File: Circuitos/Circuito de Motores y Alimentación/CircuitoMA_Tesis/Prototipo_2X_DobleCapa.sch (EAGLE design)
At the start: 28 parts, among them Q1 IRLZ44Z, Q2 IRLZ44Z, Q3 IRLZ44Z, Q4 IRLZ44Z, X1 22-23-2021

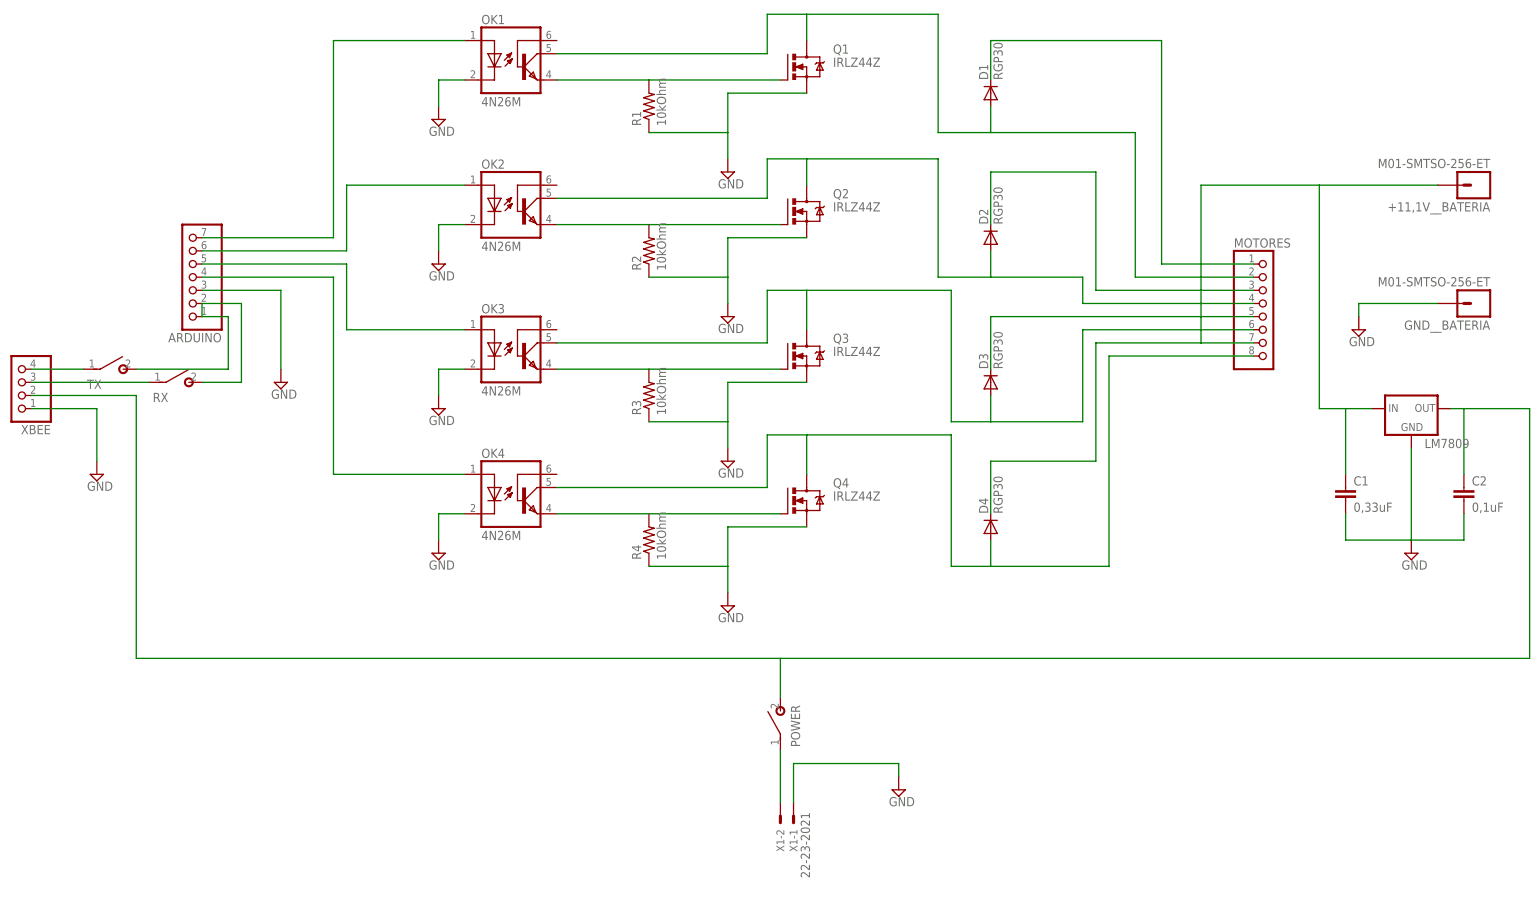
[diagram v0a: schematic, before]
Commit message: Circuito
Circuito de motores y alimentación doble capa
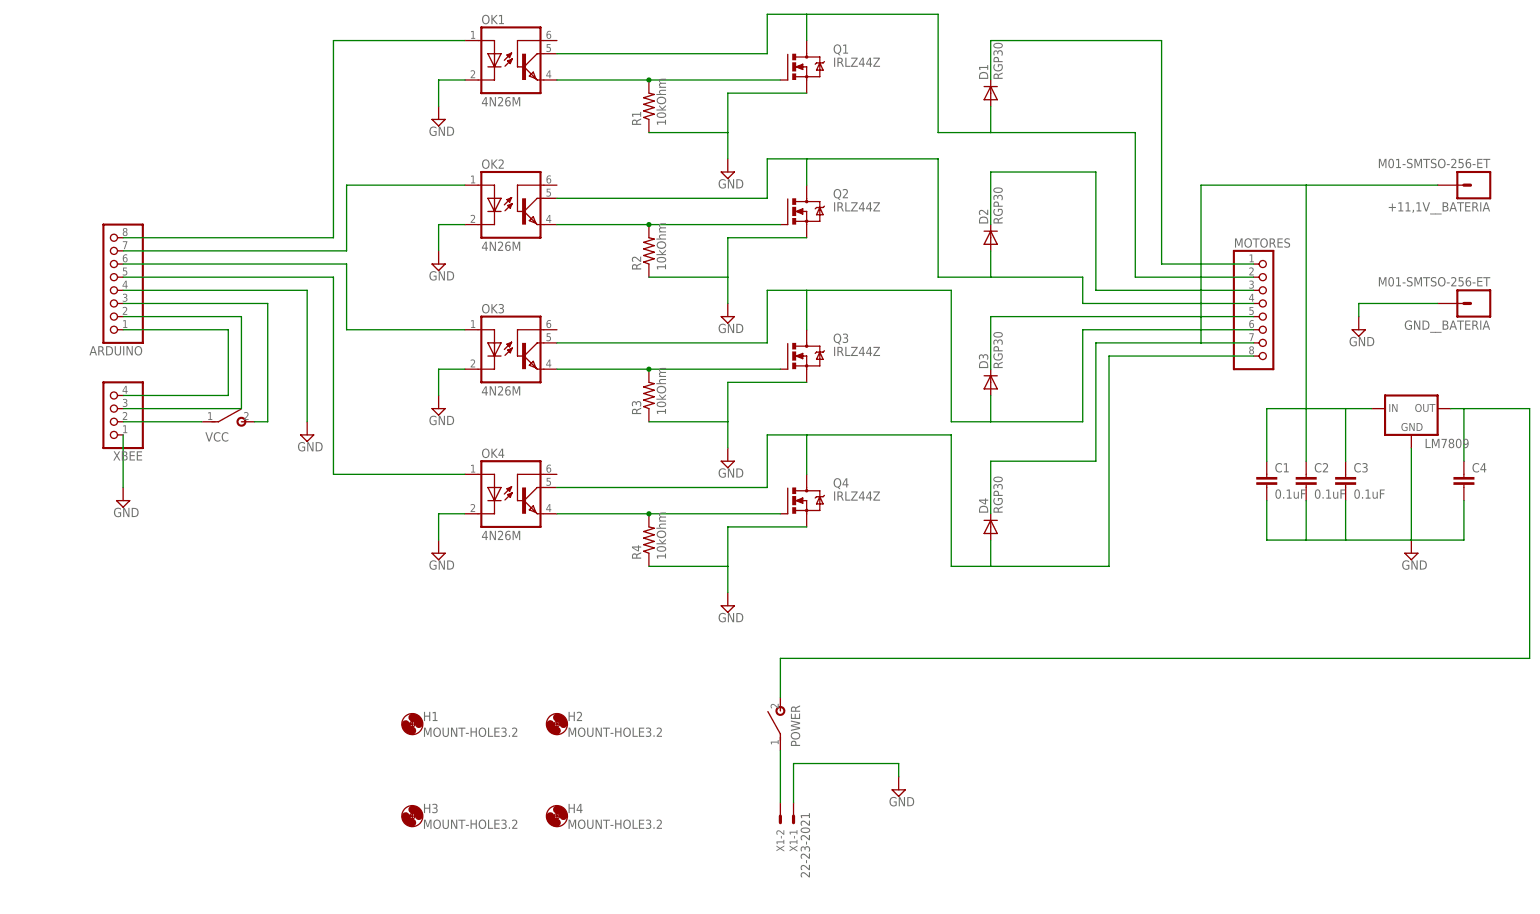
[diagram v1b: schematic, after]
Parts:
- removed RX, TX: SPST, gm-switches:SPST
- added C3: 0.1uF, SparkFun-Capacitors:0.1UF-50V-20%(PTH)KIT-EZ
- added C4: (no value), SparkFun-Capacitors:0.1UF-50V-20%(PTH)KIT-EZ
- added H1, H2, H3, H4: MOUNT-HOLE3.2, holes:MOUNT-HOLE3.2
- added VCC: SPST, gm-switches:SPST
- ARDUINO: device pinhead:PINHD-1X7/90 -> pinhead:PINHD-1X8/90
- C1: value 0,33uF -> 0.1uF; device rcl:C-EU050-030X075 -> SparkFun-Capacitors:0.1UF-50V-20%(PTH)KIT-EZ; PROD_ID (none) -> CAP-08370
- C2: value 0,1uF -> 0.1uF; device rcl:C-EU050-030X075 -> SparkFun-Capacitors:0.1UF-50V-20%(PTH)KIT-EZ; PROD_ID (none) -> CAP-08370
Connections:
- new net N$20: ARDUINO.3, VCC.S
- net GND: now also ARDUINO.4, C3.2, C4.2; no longer ARDUINO.3
- net N$1: now also ARDUINO.8; no longer ARDUINO.7
- net N$11: now also R4.2
- net N$12: now also C2.1, C3.1
- net N$13: now also ARDUINO.2; no longer RX.P
- net N$2: now also ARDUINO.7; no longer ARDUINO.6
- net N$3: now also ARDUINO.6; no longer ARDUINO.5
- net N$4: now also ARDUINO.5; no longer ARDUINO.4
- net N$5: now also ARDUINO.1; no longer TX.P
- net N$6: now also C4.1; no longer C2.1, XBEE.2
- net N$7: now also VCC.P, XBEE.2; no longer ARDUINO.1, ARDUINO.2, RX.S, TX.S
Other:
- moved on the sheet: C1, C2, XBEE

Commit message: Circuito
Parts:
- removed POWER, VCC: SPST, gm-switches:SPST
- removed X1: 22-23-2021, con-molex:22-23-2021
- added JP1: (no value), pinhead:PINHD-1X2
- added JP2: (no value), pinhead:PINHD-1X2/90
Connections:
- removed net N$6: C4.1, LM7809.OUT, POWER.S
- net GND: now also JP2.1; no longer X1-1.S
- net N$18: now also C4.1, JP2.2, LM7809.OUT; no longer POWER.P, X1-2.S
- net N$20: now also JP1.1; no longer VCC.S
- net N$7: now also JP1.2; no longer VCC.P
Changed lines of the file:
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@@
 <part name="GND__BATERIA" library="SparkFun-Connectors" deviceset="M01" device="-SMTSO-256-ET"/>
 <part name="SUPPLY12" library="supply2" deviceset="GND" device=""/>
-<part name="POWER" library="gm-switches" deviceset="SPST" device=""/>
-<part name="X1" library="con-molex" deviceset="22-23-2021" device=""/>
 <part name="SUPPLY13" library="supply2" deviceset="GND" device=""/>
 <part name="R4" library="rcl" deviceset="R-US_" device="0207/7" value="10kOhm"/>
 <part name="ARDUINO" library="pinhead" deviceset="PINHD-1X8" device="/90"/>
 <part name="R1" library="rcl" deviceset="R-US_" device="0207/7" value="10kOhm"/>
-<part name="VCC" library="gm-switches" deviceset="SPST" device=""/>
 <part name="C3" library="SparkFun-Capacitors" deviceset="0.1UF-50V-20%(PTH)" device="KIT-EZ" value="0.1uF"/>
 <part name="C1" library="SparkFun-Capacitors" deviceset="0.1UF-50V-20%(PTH)" device="KIT-EZ" value="0.1uF">
@@
 <part name="H3" library="holes" deviceset="MOUNT-HOLE" device="3.2"/>
 <part name="H4" library="holes" deviceset="MOUNT-HOLE" device="3.2"/>
+<part name="JP2" library="pinhead" deviceset="PINHD-1X2" device="/90"/>
+<part name="JP1" library="pinhead" deviceset="PINHD-1X2" device=""/>
 </parts>
 <sheets>
@@
 <instance part="GND__BATERIA" gate="G$1" x="208.28" y="35.56" rot="R180"/>
 <instance part="SUPPLY12" gate="GND" x="185.42" y="30.48"/>
-<instance part="POWER" gate="G$1" x="73.66" y="-45.72"/>
-<instance part="X1" gate="-1" x="76.2" y="-63.5" rot="R270"/>
-<instance part="X1" gate="-2" x="73.66" y="-63.5" rot="MR270"/>
 <instance part="SUPPLY13" gate="GND" x="96.52" y="-58.42"/>
 <instance part="R4" gate="G$1" x="48.26" y="-10.16" rot="R90"/>
 <instance part="ARDUINO" gate="A" x="-55.88" y="40.64" rot="R180"/>
 <instance part="R1" gate="G$1" x="48.26" y="73.66" rot="R90"/>
-<instance part="VCC" gate="G$1" x="-33.02" y="12.7" rot="R270"/>
 <instance part="C3" gate="G$1" x="182.88" y="0"/>
 <instance part="C1" gate="G$1" x="167.64" y="0"/>
@@
 <instance part="H3" gate="G$1" x="2.54" y="-63.5"/>
 <instance part="H4" gate="G$1" x="30.48" y="-63.5"/>
+<instance part="JP2" gate="G$1" x="71.12" y="-60.96" rot="R270"/>
+<instance part="JP1" gate="G$1" x="-33.02" y="2.54" rot="R270"/>
 </instances>
 <busses>
@@
 <wire x1="-12.7" y1="2.54" x2="12.7" y2="2.54" width="0.1524" layer="91"/>
 <pinref part="ARDUINO" gate="A" pin="5"/>
-</segment>
-</net>
-<net name="N$6" class="0">
-<segment>
-<pinref part="LM7809" gate="A" pin="OUT"/>
-<wire x1="203.2" y1="15.24" x2="205.74" y2="15.24" width="0.1524" layer="91"/>
-<wire x1="205.74" y1="15.24" x2="205.74" y2="5.08" width="0.1524" layer="91"/>
-<wire x1="73.66" y1="-33.02" x2="218.44" y2="-33.02" width="0.1524" layer="91"/>
-<wire x1="218.44" y1="-33.02" x2="218.44" y2="15.24" width="0.1524" layer="91"/>
-<wire x1="218.44" y1="15.24" x2="205.74" y2="15.24" width="0.1524" layer="91"/>
-<pinref part="POWER" gate="G$1" pin="S"/>
-<wire x1="73.66" y1="-40.64" x2="73.66" y2="-33.02" width="0.1524" layer="91"/>
-<pinref part="C4" gate="G$1" pin="1"/>
 </segment>
 </net>
@@
 </segment>
 <segment>
-<pinref part="X1" gate="-1" pin="S"/>
-<wire x1="76.2" y1="-60.96" x2="76.2" y2="-53.34" width="0.1524" layer="91"/>
-<wire x1="76.2" y1="-53.34" x2="96.52" y2="-53.34" width="0.1524" layer="91"/>
+<wire x1="73.66" y1="-53.34" x2="96.52" y2="-53.34" width="0.1524" layer="91"/>
 <pinref part="SUPPLY13" gate="GND" pin="GND"/>
 <wire x1="96.52" y1="-53.34" x2="96.52" y2="-55.88" width="0.1524" layer="91"/>
+<pinref part="JP2" gate="G$1" pin="1"/>
+<wire x1="73.66" y1="-53.34" x2="73.66" y2="-58.42" width="0.1524" layer="91"/>
 </segment>
 <segment>
@@
 <net name="N$18" class="0">
 <segment>
-<pinref part="POWER" gate="G$1" pin="P"/>
-<pinref part="X1" gate="-2" pin="S"/>
-<wire x1="73.66" y1="-50.8" x2="73.66" y2="-60.96" width="0.1524" layer="91"/>
+<pinref part="LM7809" gate="A" pin="OUT"/>
+<wire x1="203.2" y1="15.24" x2="205.74" y2="15.24" width="0.1524" layer="91"/>
+<wire x1="205.74" y1="15.24" x2="205.74" y2="5.08" width="0.1524" layer="91"/>
+<wire x1="71.12" y1="-33.02" x2="218.44" y2="-33.02" width="0.1524" layer="91"/>
+<wire x1="218.44" y1="-33.02" x2="218.44" y2="15.24" width="0.1524" layer="91"/>
+<wire x1="218.44" y1="15.24" x2="205.74" y2="15.24" width="0.1524" layer="91"/>
+<pinref part="C4" gate="G$1" pin="1"/>
+<pinref part="JP2" gate="G$1" pin="2"/>
+<wire x1="71.12" y1="-33.02" x2="71.12" y2="-58.42" width="0.1524" layer="91"/>
 </segment>
 </net>
 <net name="N$20" class="0">
 <segment>
-<wire x1="-27.94" y1="12.7" x2="-25.4" y2="12.7" width="0.1524" layer="91"/>
 <wire x1="-25.4" y1="12.7" x2="-25.4" y2="35.56" width="0.1524" layer="91"/>
 <pinref part="ARDUINO" gate="A" pin="3"/>
 <wire x1="-25.4" y1="35.56" x2="-53.34" y2="35.56" width="0.1524" layer="91"/>
-<pinref part="VCC" gate="G$1" pin="S"/>
+<pinref part="JP1" gate="G$1" pin="1"/>
+<wire x1="-30.48" y1="5.08" x2="-30.48" y2="12.7" width="0.1524" layer="91"/>
+<wire x1="-30.48" y1="12.7" x2="-25.4" y2="12.7" width="0.1524" layer="91"/>
 </segment>
 </net>
@@
 <segment>
 <pinref part="XBEE" gate="A" pin="2"/>
-<wire x1="-53.34" y1="12.7" x2="-38.1" y2="12.7" width="0.1524" layer="91"/>
-<pinref part="VCC" gate="G$1" pin="P"/>
-</segment>
-</net>
+<wire x1="-53.34" y1="12.7" x2="-33.02" y2="12.7" width="0.1524" layer="91"/>
+<pinref part="JP1" gate="G$1" pin="2"/>
+<wire x1="-33.02" y1="12.7" x2="-33.02" y2="5.08" width="0.1524" layer="91"/>
+</segment>
+</net>

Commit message: Circuito
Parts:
- added R5, R6, R7, R8: 470KOhm, resistor:R-US_0207/7
- R1, R2, R3, R4: value 10kOhm -> 10Ohm
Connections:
- new net N$19: OK2.BAS, R5.2
- new net N$21: OK3.BAS, R6.2
- new net N$22: OK4.BAS, R8.2
- new net N$6: OK1.BAS, R7.2
- net GND: now also R5.1, R6.1, R7.1, R8.1
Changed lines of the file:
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@@
 <part name="SUPPLY12" library="supply2" deviceset="GND" device=""/>
 <part name="SUPPLY13" library="supply2" deviceset="GND" device=""/>
-<part name="R4" library="rcl" deviceset="R-US_" device="0207/7" value="10kOhm"/>
+<part name="R4" library="rcl" deviceset="R-US_" device="0207/7" value="10Ohm"/>
 <part name="ARDUINO" library="pinhead" deviceset="PINHD-1X8" device="/90"/>
-<part name="R1" library="rcl" deviceset="R-US_" device="0207/7" value="10kOhm"/>
+<part name="R1" library="rcl" deviceset="R-US_" device="0207/7" value="10Ohm"/>
 <part name="C3" library="SparkFun-Capacitors" deviceset="0.1UF-50V-20%(PTH)" device="KIT-EZ" value="0.1uF"/>
 <part name="C1" library="SparkFun-Capacitors" deviceset="0.1UF-50V-20%(PTH)" device="KIT-EZ" value="0.1uF">
@@
 <attribute name="PROD_ID" value="CAP-08370"/>
 </part>
-<part name="R2" library="rcl" deviceset="R-US_" device="0207/7" value="10kOhm"/>
-<part name="R3" library="rcl" deviceset="R-US_" device="0207/7" value="10kOhm"/>
+<part name="R2" library="rcl" deviceset="R-US_" device="0207/7" value="10Ohm"/>
+<part name="R3" library="rcl" deviceset="R-US_" device="0207/7" value="10Ohm"/>
 <part name="H1" library="holes" deviceset="MOUNT-HOLE" device="3.2"/>
 <part name="H2" library="holes" deviceset="MOUNT-HOLE" device="3.2"/>
@@
 <part name="JP2" library="pinhead" deviceset="PINHD-1X2" device="/90"/>
 <part name="JP1" library="pinhead" deviceset="PINHD-1X2" device=""/>
+<part name="R5" library="resistor" deviceset="R-US_" device="0207/7" value="470KOhm"/>
+<part name="R6" library="resistor" deviceset="R-US_" device="0207/7" value="470KOhm"/>
+<part name="R7" library="resistor" deviceset="R-US_" device="0207/7" value="470KOhm"/>
+<part name="R8" library="resistor" deviceset="R-US_" device="0207/7" value="470KOhm"/>
 </parts>
 <sheets>
@@
 <instance part="D4" gate="1" x="114.3" y="-7.62" rot="R90"/>
 <instance part="SUPPLY1" gate="GND" x="195.58" y="-12.7"/>
-<instance part="SUPPLY2" gate="GND" x="63.5" y="60.96"/>
-<instance part="SUPPLY3" gate="GND" x="63.5" y="33.02"/>
-<instance part="SUPPLY4" gate="GND" x="63.5" y="5.08"/>
-<instance part="SUPPLY5" gate="GND" x="63.5" y="-22.86"/>
+<instance part="SUPPLY2" gate="GND" x="63.5" y="63.5"/>
+<instance part="SUPPLY3" gate="GND" x="63.5" y="35.56"/>
+<instance part="SUPPLY4" gate="GND" x="63.5" y="7.62"/>
+<instance part="SUPPLY5" gate="GND" x="63.5" y="-20.32"/>
 <instance part="SUPPLY6" gate="GND" x="-53.34" y="-2.54"/>
 <instance part="SUPPLY7" gate="GND" x="-17.78" y="10.16"/>
@@
 <instance part="JP2" gate="G$1" x="71.12" y="-60.96" rot="R270"/>
 <instance part="JP1" gate="G$1" x="-33.02" y="2.54" rot="R270"/>
+<instance part="R5" gate="G$1" x="40.64" y="58.42" rot="R180"/>
+<instance part="R6" gate="G$1" x="40.64" y="30.48" rot="R180"/>
+<instance part="R7" gate="G$1" x="40.64" y="86.36" rot="R180"/>
+<instance part="R8" gate="G$1" x="40.64" y="2.54" rot="R180"/>
 </instances>
 <busses>
@@
 <pinref part="SUPPLY2" gate="GND" pin="GND"/>
 <wire x1="48.26" y1="68.58" x2="63.5" y2="68.58" width="0.1524" layer="91"/>
-<wire x1="63.5" y1="68.58" x2="63.5" y2="63.5" width="0.1524" layer="91"/>
+<wire x1="63.5" y1="68.58" x2="63.5" y2="66.04" width="0.1524" layer="91"/>
 <pinref part="Q1" gate="G$1" pin="S"/>
 <wire x1="78.74" y1="76.2" x2="63.5" y2="76.2" width="0.1524" layer="91"/>
 <wire x1="63.5" y1="76.2" x2="63.5" y2="68.58" width="0.1524" layer="91"/>
 <pinref part="R1" gate="G$1" pin="1"/>
+<pinref part="R7" gate="G$1" pin="1"/>
+<wire x1="45.72" y1="86.36" x2="63.5" y2="86.36" width="0.1524" layer="91"/>
+<wire x1="63.5" y1="86.36" x2="63.5" y2="76.2" width="0.1524" layer="91"/>
 </segment>
 <segment>
 <pinref part="SUPPLY3" gate="GND" pin="GND"/>
 <wire x1="48.26" y1="40.64" x2="63.5" y2="40.64" width="0.1524" layer="91"/>
-<wire x1="63.5" y1="40.64" x2="63.5" y2="35.56" width="0.1524" layer="91"/>
+<wire x1="63.5" y1="40.64" x2="63.5" y2="38.1" width="0.1524" layer="91"/>
 <pinref part="Q2" gate="G$1" pin="S"/>
 <wire x1="78.74" y1="48.26" x2="63.5" y2="48.26" width="0.1524" layer="91"/>
 <wire x1="63.5" y1="48.26" x2="63.5" y2="40.64" width="0.1524" layer="91"/>
 <pinref part="R2" gate="G$1" pin="1"/>
+<pinref part="R5" gate="G$1" pin="1"/>
+<wire x1="45.72" y1="58.42" x2="63.5" y2="58.42" width="0.1524" layer="91"/>
+<wire x1="63.5" y1="58.42" x2="63.5" y2="48.26" width="0.1524" layer="91"/>
 </segment>
 <segment>
 <pinref part="SUPPLY4" gate="GND" pin="GND"/>
 <wire x1="48.26" y1="12.7" x2="63.5" y2="12.7" width="0.1524" layer="91"/>
-<wire x1="63.5" y1="12.7" x2="63.5" y2="7.62" width="0.1524" layer="91"/>
+<wire x1="63.5" y1="12.7" x2="63.5" y2="10.16" width="0.1524" layer="91"/>
 <pinref part="Q3" gate="G$1" pin="S"/>
 <wire x1="78.74" y1="20.32" x2="63.5" y2="20.32" width="0.1524" layer="91"/>
 <wire x1="63.5" y1="20.32" x2="63.5" y2="12.7" width="0.1524" layer="91"/>
 <pinref part="R3" gate="G$1" pin="1"/>
+<pinref part="R6" gate="G$1" pin="1"/>
+<wire x1="45.72" y1="30.48" x2="63.5" y2="30.48" width="0.1524" layer="91"/>
+<wire x1="63.5" y1="30.48" x2="63.5" y2="20.32" width="0.1524" layer="91"/>
 </segment>
 <segment>
 <pinref part="SUPPLY5" gate="GND" pin="GND"/>
 <wire x1="48.26" y1="-15.24" x2="63.5" y2="-15.24" width="0.1524" layer="91"/>
-<wire x1="63.5" y1="-15.24" x2="63.5" y2="-20.32" width="0.1524" layer="91"/>
+<wire x1="63.5" y1="-15.24" x2="63.5" y2="-17.78" width="0.1524" layer="91"/>
 <pinref part="Q4" gate="G$1" pin="S"/>
 <wire x1="78.74" y1="-7.62" x2="63.5" y2="-7.62" width="0.1524" layer="91"/>
 <wire x1="63.5" y1="-7.62" x2="63.5" y2="-15.24" width="0.1524" layer="91"/>
 <pinref part="R4" gate="G$1" pin="1"/>
+<pinref part="R8" gate="G$1" pin="1"/>
+<wire x1="45.72" y1="2.54" x2="63.5" y2="2.54" width="0.1524" layer="91"/>
+<wire x1="63.5" y1="2.54" x2="63.5" y2="-7.62" width="0.1524" layer="91"/>
 </segment>
 <segment>
@@
 </segment>
 </net>
+<net name="N$6" class="0">
+<segment>
+<pinref part="OK1" gate="G$1" pin="BAS"/>
+<pinref part="R7" gate="G$1" pin="2"/>
+<wire x1="30.48" y1="86.36" x2="35.56" y2="86.36" width="0.1524" layer="91"/>
+</segment>
+</net>
+<net name="N$19" class="0">
+<segment>
+<pinref part="OK2" gate="G$1" pin="BAS"/>
+<pinref part="R5" gate="G$1" pin="2"/>
+<wire x1="30.48" y1="58.42" x2="35.56" y2="58.42" width="0.1524" layer="91"/>
+</segment>
+</net>
+<net name="N$21" class="0">
+<segment>
+<pinref part="OK3" gate="G$1" pin="BAS"/>
+<pinref part="R6" gate="G$1" pin="2"/>
+<wire x1="30.48" y1="30.48" x2="35.56" y2="30.48" width="0.1524" layer="91"/>
+</segment>
+</net>
+<net name="N$22" class="0">
+<segment>
+<pinref part="OK4" gate="G$1" pin="BAS"/>
+<pinref part="R8" gate="G$1" pin="2"/>
+<wire x1="30.48" y1="2.54" x2="35.56" y2="2.54" width="0.1524" layer="91"/>
+</segment>
+</net>

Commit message: Circuito
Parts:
- R1, R2, R3, R4: value 10Ohm -> 1KOhm
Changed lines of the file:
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@@
 <part name="SUPPLY12" library="supply2" deviceset="GND" device=""/>
 <part name="SUPPLY13" library="supply2" deviceset="GND" device=""/>
-<part name="R4" library="rcl" deviceset="R-US_" device="0207/7" value="10Ohm"/>
+<part name="R4" library="rcl" deviceset="R-US_" device="0207/7" value="1KOhm"/>
 <part name="ARDUINO" library="pinhead" deviceset="PINHD-1X8" device="/90"/>
-<part name="R1" library="rcl" deviceset="R-US_" device="0207/7" value="10Ohm"/>
+<part name="R1" library="rcl" deviceset="R-US_" device="0207/7" value="1KOhm"/>
 <part name="C3" library="SparkFun-Capacitors" deviceset="0.1UF-50V-20%(PTH)" device="KIT-EZ" value="0.1uF"/>
 <part name="C1" library="SparkFun-Capacitors" deviceset="0.1UF-50V-20%(PTH)" device="KIT-EZ" value="0.1uF">
@@
 <attribute name="PROD_ID" value="CAP-08370"/>
 </part>
-<part name="R2" library="rcl" deviceset="R-US_" device="0207/7" value="10Ohm"/>
-<part name="R3" library="rcl" deviceset="R-US_" device="0207/7" value="10Ohm"/>
+<part name="R2" library="rcl" deviceset="R-US_" device="0207/7" value="1KOhm"/>
+<part name="R3" library="rcl" deviceset="R-US_" device="0207/7" value="1KOhm"/>
 <part name="H1" library="holes" deviceset="MOUNT-HOLE" device="3.2"/>
 <part name="H2" library="holes" deviceset="MOUNT-HOLE" device="3.2"/>
